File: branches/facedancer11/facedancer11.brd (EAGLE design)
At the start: 71.1 x 23.5 mm, 20 parts, among them CN1 HOST, CN2 VICTIM, Q1 12MHz, U1 F261X---PM64, U2 FT232RL-BASICSSOP, U3 MAX3420ELQFP32

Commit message: Facedancer11 pieces.
git-svn-id: https://svn.code.sf.net/p/goodfet/code@1181 12e2690d-a6be-4b82-a7b7-67c4a43b65c8
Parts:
- CN2: value VICTIM -> TARGET
- moved C6 2.81 mm to (53.8, 7.20)
- moved C7 1.61 mm to (42.4, 7.80)
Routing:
- net N$4: track 12.0 -> 14.7 mm
- net N$3: track 8.26 -> 10.1 mm
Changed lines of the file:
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@@
 <attribute name="VALUE" x="57.8635" y="0.18" size="1.27" layer="27" ratio="10" rot="R90"/>
 </element>
-<element name="CN2" library="adafruit" package="USB-MINIB" value="VICTIM" x="66.3575" y="9.8425" smashed="yes" rot="R90">
+<element name="CN2" library="adafruit" package="USB-MINIB" value="TARGET" x="66.3575" y="9.8425" smashed="yes" rot="R90">
 <attribute name="VALUE" x="62.45" y="15.775" size="1.27" layer="27"/>
 </element>
@@
 <attribute name="VALUE" x="55.36" y="16.6825" size="0.4064" layer="27" font="vector"/>
 </element>
-<element name="C6" library="rcl" package="C0603" value="18pF" x="51" y="7.4" smashed="yes" rot="R180">
-<attribute name="NAME" x="52.565" y="7.035" size="0.4064" layer="25" font="vector"/>
-</element>
-<element name="C7" library="rcl" package="C0603" value="18pF" x="44" y="7.6" smashed="yes">
-<attribute name="NAME" x="43.365" y="8.235" size="0.4064" layer="25" font="vector"/>
-<attribute name="VALUE" x="43.365" y="8.695" size="0.4064" layer="27" font="fixed"/>
+<element name="C6" library="rcl" package="C0603" value="18pF" x="53.8" y="7.2" smashed="yes" rot="R180">
+<attribute name="NAME" x="55.365" y="6.835" size="0.4064" layer="25" font="vector"/>
+</element>
+<element name="C7" library="rcl" package="C0603" value="18pF" x="42.4" y="7.8" smashed="yes">
+<attribute name="NAME" x="41.765" y="8.435" size="0.4064" layer="25" font="vector"/>
+<attribute name="VALUE" x="41.765" y="8.895" size="0.4064" layer="27" font="fixed"/>
 </element>
 </elements>
@@
 <contactref element="C7" pad="1"/>
 <contactref element="C6" pad="1"/>
-<wire x1="43.15" y1="7.6" x2="42.15" y2="7.55" width="0.254" layer="1"/>
-<wire x1="42.15" y1="7.55" x2="41" y2="6.8" width="0.254" layer="1"/>
-<via x="41" y="6.8" extent="1-16" drill="0.6"/>
-<wire x1="51.85" y1="7.4" x2="53.6" y2="7.4" width="0.254" layer="1"/>
-<wire x1="53.6" y1="7.4" x2="54" y2="8.2" width="0.254" layer="1"/>
-<via x="54" y="8.2" extent="1-16" drill="0.6"/>
+<wire x1="54.65" y1="7.2" x2="56.4" y2="6.8" width="0.254" layer="1"/>
+<wire x1="56.4" y1="6.8" x2="56.8" y2="6.4" width="0.254" layer="1"/>
+<via x="56.8" y="6.4" extent="1-16" drill="0.6"/>
 <contactref element="U3" pad="P18"/>
 <contactref element="U3" pad="P19"/>
@@
 <wire x1="53.3775" y1="14.435" x2="55.3675" y2="14.435" width="0.3048" layer="1"/>
 <wire x1="55.3675" y1="14.435" x2="56.1875" y2="15.255" width="0.3048" layer="1"/>
+<wire x1="41.55" y1="7.8" x2="40.6" y2="6.85" width="0.3048" layer="1"/>
+<wire x1="40.6" y1="6.85" x2="40.6" y2="6" width="0.3048" layer="1"/>
+<via x="40.6" y="6" extent="1-16" drill="0.6"/>
 </signal>
 <signal name="N$1">
@@
 <contactref element="Q1" pad="1"/>
 <contactref element="U3" pad="P26"/>
-<wire x1="46.7425" y1="8.7" x2="46.7425" y2="7.4" width="0.254" layer="1"/>
-<wire x1="46.7425" y1="7.4" x2="46.7425" y2="6.801" width="0.254" layer="1"/>
-<wire x1="46.7425" y1="6.801" x2="44.069" y2="3.3275" width="0.254" layer="1"/>
+<wire x1="46.7425" y1="8.7" x2="46.7425" y2="6.801" width="0.254" layer="1"/>
+<wire x1="46.7425" y1="6.801" x2="46.592334375" y2="6.6059" width="0.254" layer="1"/>
 <contactref element="C7" pad="2"/>
-<wire x1="44.85" y1="7.6" x2="46.5425" y2="7.6" width="0.254" layer="1"/>
-<wire x1="46.5425" y1="7.6" x2="46.7425" y2="7.4" width="0.254" layer="1"/>
+<wire x1="46.592334375" y1="6.6059" x2="44.069" y2="3.3275" width="0.254" layer="1"/>
+<wire x1="43.25" y1="7.8" x2="44.4441" y2="6.6059" width="0.3048" layer="1"/>
+<wire x1="44.4441" y1="6.6059" x2="46.592334375" y2="6.6059" width="0.3048" layer="1"/>
 </signal>
 <signal name="N$4">
@@
 <contactref element="C6" pad="2"/>
 <wire x1="47.5425" y1="7.2325" x2="49.9825" y2="7.2325" width="0.254" layer="1"/>
-<wire x1="49.9825" y1="7.2325" x2="50.15" y2="7.4" width="0.254" layer="1"/>
+<wire x1="49.9825" y1="7.2325" x2="52.95" y2="7.2" width="0.254" layer="1"/>
 </signal>
 <signal name="N$5">

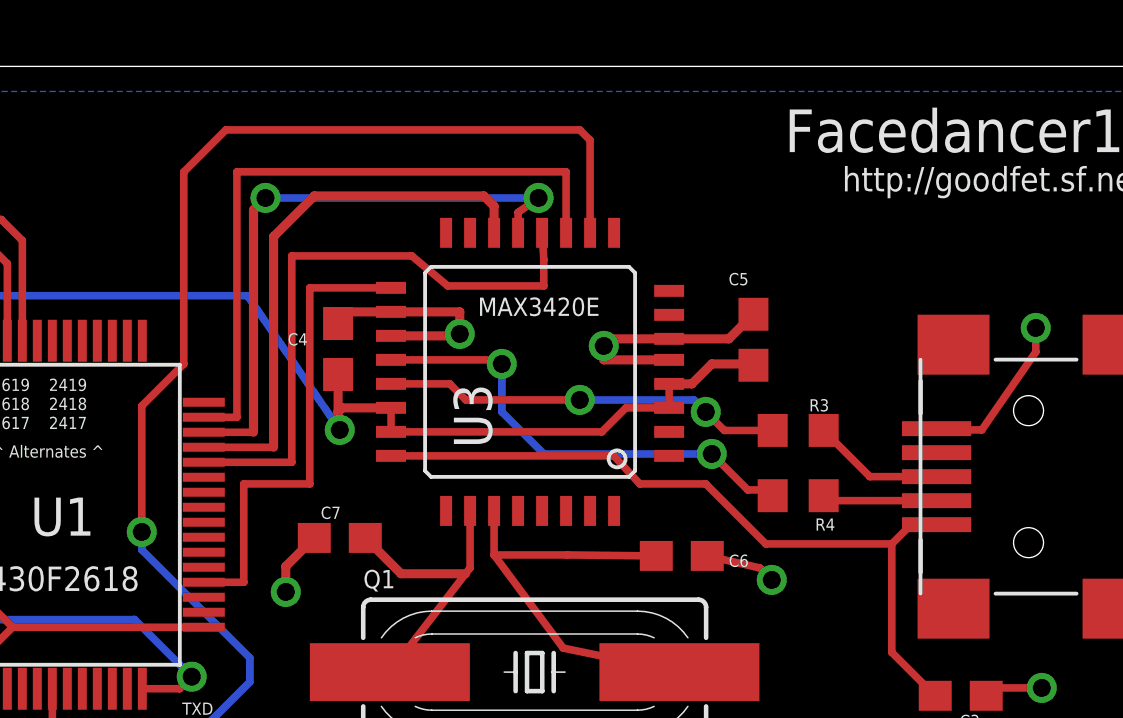
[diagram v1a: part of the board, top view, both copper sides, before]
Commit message: Improved Facedancer11 layout.
git-svn-id: https://svn.code.sf.net/p/goodfet/code@1184 12e2690d-a6be-4b82-a7b7-67c4a43b65c8
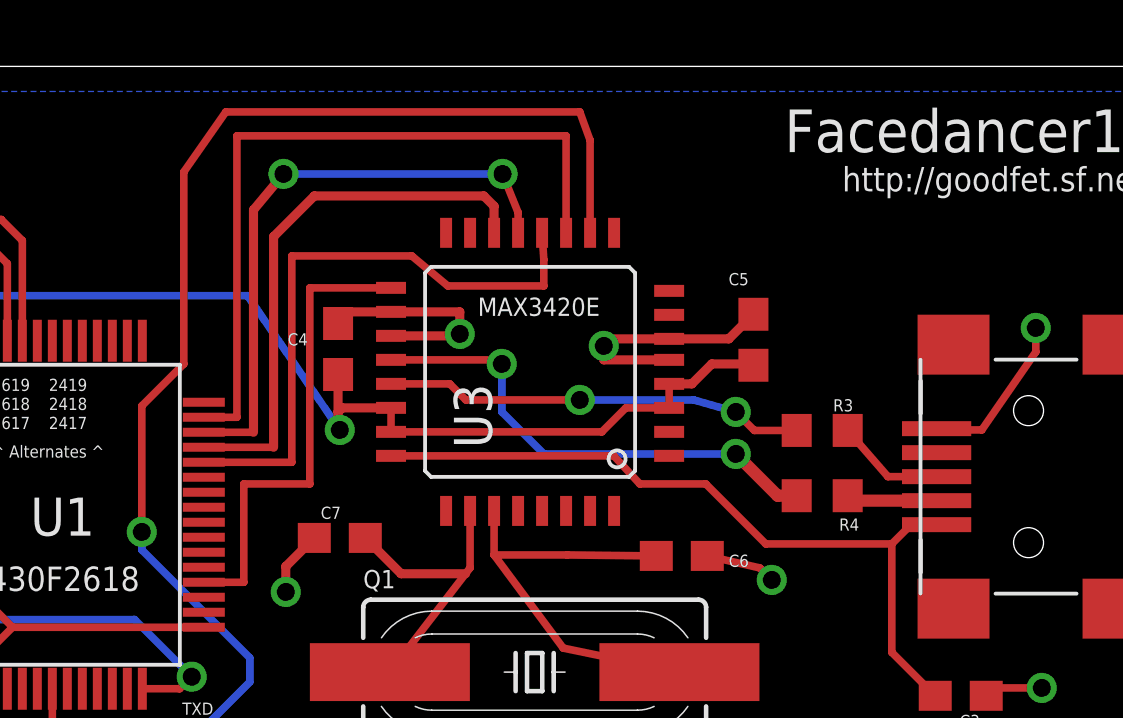
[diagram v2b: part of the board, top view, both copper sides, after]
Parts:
- moved R3 0.80 mm to (58.5, 11.4)
- moved R4 0.80 mm to (58.5, 9.21)
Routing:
- net SCLK: track 22.3 -> 24.7 mm
- net !RST: track 45.5 -> 46.5 mm
- net N$10: track 3.98 -> 3.13 mm
- net N$11: track 4.40 -> 3.66 mm
- net N$9: track 15.6 -> 16.3 mm
- net N$5: track 13.4 -> 14.1 mm
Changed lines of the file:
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@@
 <attribute name="VALUE" x="62.45" y="15.775" size="1.27" layer="27"/>
 </element>
-<element name="R3" library="rcl" package="R0603" value="33" x="57.68" y="11.3825" smashed="yes">
-<attribute name="NAME" x="58.045" y="12.0175" size="0.4064" layer="25" font="vector"/>
-<attribute name="VALUE" x="58.045" y="12.6775" size="0.4064" layer="27" font="vector"/>
-</element>
-<element name="R4" library="rcl" package="R0603" value="33" x="57.68" y="9.2075" smashed="yes">
-<attribute name="NAME" x="58.245" y="8.0425" size="0.4064" layer="25" font="vector"/>
-<attribute name="VALUE" x="58.245" y="7.5025" size="0.4064" layer="27" font="vector"/>
+<element name="R3" library="rcl" package="R0603" value="33" x="58.48" y="11.3825" smashed="yes">
+<attribute name="NAME" x="58.845" y="12.0175" size="0.4064" layer="25" font="vector"/>
+<attribute name="VALUE" x="58.845" y="12.6775" size="0.4064" layer="27" font="vector"/>
+</element>
+<element name="R4" library="rcl" package="R0603" value="33" x="58.48" y="9.2075" smashed="yes">
+<attribute name="NAME" x="59.045" y="8.0425" size="0.4064" layer="25" font="vector"/>
+<attribute name="VALUE" x="59.045" y="7.5025" size="0.4064" layer="27" font="vector"/>
 </element>
 <element name="C3" library="rcl" package="C0603" value="1.0uF" x="63.0975" y="2.5375" smashed="yes" rot="R180">
@@
 <contactref element="U3" pad="P13"/>
 <wire x1="37.8675" y1="11.3225" x2="39.5225" y2="11.3225" width="0.254" layer="1"/>
-<via x="39.9225" y="19.1325" extent="1-16" drill="0.6"/>
-<wire x1="39.9225" y1="19.1325" x2="49.025" y2="19.1325" width="0.254" layer="16"/>
+<via x="40.5225" y="19.9325" extent="1-16" drill="0.6"/>
+<wire x1="40.5225" y1="19.9325" x2="47.825" y2="19.9325" width="0.254" layer="16"/>
 <wire x1="48.3425" y1="17.97" x2="48.3425" y2="18.65" width="0.254" layer="1"/>
-<wire x1="48.3425" y1="18.65" x2="49.025" y2="19.1325" width="0.254" layer="1"/>
-<via x="49.025" y="19.1325" extent="1-16" drill="0.6"/>
+<wire x1="48.3425" y1="18.65" x2="47.825" y2="19.9325" width="0.254" layer="1"/>
+<via x="47.825" y="19.9325" extent="1-16" drill="0.6"/>
 <wire x1="39.5225" y1="11.3225" x2="39.5225" y2="18.7325" width="0.3048" layer="1"/>
-<wire x1="39.5225" y1="18.7325" x2="39.9225" y2="19.1325" width="0.3048" layer="1"/>
+<wire x1="39.5225" y1="18.7325" x2="40.5225" y2="19.9325" width="0.3048" layer="1"/>
 </signal>
 <signal name="SCLK">
@@
 <contactref element="U3" pad="P11"/>
 <wire x1="37.8675" y1="11.8225" x2="38.97" y2="11.8225" width="0.254" layer="1"/>
-<wire x1="38.97" y1="11.8225" x2="38.97" y2="20.0025" width="0.254" layer="1"/>
-<wire x1="38.97" y1="20.0025" x2="49.9425" y2="20.0025" width="0.254" layer="1"/>
-<wire x1="49.9425" y1="20.0025" x2="49.9425" y2="17.97" width="0.254" layer="1"/>
+<wire x1="38.97" y1="11.8225" x2="38.97" y2="21.2025" width="0.254" layer="1"/>
+<wire x1="38.97" y1="21.2025" x2="49.9425" y2="21.2025" width="0.254" layer="1"/>
+<wire x1="49.9425" y1="21.2025" x2="49.9425" y2="17.97" width="0.254" layer="1"/>
 </signal>
 <signal name="VCC">
@@
 <contactref element="U3" pad="P10"/>
 <wire x1="50.7425" y1="17.97" x2="50.7425" y2="21.0575" width="0.254" layer="1"/>
-<wire x1="50.7425" y1="21.0575" x2="50.4" y2="21.4" width="0.254" layer="1"/>
-<wire x1="50.4" y1="21.4" x2="38.6" y2="21.4" width="0.254" layer="1"/>
-<wire x1="38.6" y1="21.4" x2="37.2" y2="20" width="0.254" layer="1"/>
+<wire x1="50.7425" y1="21.0575" x2="50.4" y2="22" width="0.254" layer="1"/>
+<wire x1="50.4" y1="22" x2="38.6" y2="22" width="0.254" layer="1"/>
+<wire x1="38.6" y1="22" x2="37.2" y2="20" width="0.254" layer="1"/>
 <wire x1="37.2" y1="20" x2="37.2" y2="13.6" width="0.254" layer="1"/>
 <wire x1="37.2" y1="13.6" x2="35.8" y2="12.2" width="0.254" layer="1"/>
@@
 <via x="50.4" y="12.4" extent="1-16" drill="0.6"/>
 <wire x1="50.4" y1="12.4" x2="54.2" y2="12.4" width="0.254" layer="16"/>
-<wire x1="54.2" y1="12.4" x2="54.6" y2="12" width="0.254" layer="16"/>
-<wire x1="56.83" y1="11.3825" x2="55.2175" y2="11.3825" width="0.254" layer="1"/>
-<wire x1="55.2175" y1="11.3825" x2="54.6" y2="12" width="0.254" layer="1"/>
-<via x="54.6" y="12" extent="1-16" drill="0.6"/>
+<wire x1="54.2" y1="12.4" x2="55.6" y2="12" width="0.254" layer="16"/>
+<wire x1="57.63" y1="11.3825" x2="56.2175" y2="11.3825" width="0.254" layer="1"/>
+<wire x1="56.2175" y1="11.3825" x2="55.6" y2="12" width="0.254" layer="1"/>
+<via x="55.6" y="12" extent="1-16" drill="0.6"/>
 </signal>
 <signal name="N$9">
@@
 <wire x1="47.8" y1="13.6" x2="47.8" y2="12" width="0.254" layer="16"/>
 <wire x1="47.8" y1="12" x2="49.2" y2="10.6" width="0.254" layer="16"/>
-<wire x1="49.2" y1="10.6" x2="54.8" y2="10.6" width="0.254" layer="16"/>
-<wire x1="56.83" y1="9.2075" x2="56.83" y2="9.37" width="0.254" layer="1"/>
-<wire x1="56.83" y1="9.37" x2="56.8" y2="9.4" width="0.254" layer="1"/>
-<wire x1="56.8" y1="9.4" x2="56" y2="9.4" width="0.254" layer="1"/>
-<wire x1="56" y1="9.4" x2="54.8" y2="10.6" width="0.254" layer="1"/>
-<via x="54.8" y="10.6" extent="1-16" drill="0.6"/>
+<wire x1="49.2" y1="10.6" x2="55.6" y2="10.6" width="0.254" layer="16"/>
+<via x="55.6" y="10.6" extent="1-16" drill="0.6"/>
+<wire x1="57.63" y1="9.2075" x2="56.9925" y2="9.2075" width="0.4064" layer="1"/>
+<wire x1="56.9925" y1="9.2075" x2="55.6" y2="10.6" width="0.4064" layer="1"/>
 </signal>
 <signal name="VBCOMP">
@@
 <contactref element="CN2" pad="D-"/>
 <contactref element="R4" pad="2"/>
-<wire x1="58.53" y1="9.36" x2="58.53" y2="9.2075" width="0.254" layer="1"/>
-<wire x1="62.2935" y1="9.0425" x2="58.7575" y2="9.0425" width="0.254" layer="1"/>
-<wire x1="58.7575" y1="9.0425" x2="58.6" y2="9.2" width="0.254" layer="1"/>
-<wire x1="58.6" y1="9.2" x2="58.5375" y2="9.2" width="0.254" layer="1"/>
-<wire x1="58.5375" y1="9.2" x2="58.53" y2="9.2075" width="0.254" layer="1"/>
+<wire x1="62.2935" y1="9.0425" x2="59.33" y2="9.0425" width="0.4064" layer="1"/>
+<wire x1="59.33" y1="9.0425" x2="59.33" y2="9.2075" width="0.4064" layer="1"/>
 </signal>
 <signal name="N$11">
 <contactref element="CN2" pad="D+"/>
 <contactref element="R3" pad="2"/>
-<wire x1="62.2935" y1="9.8425" x2="60.07" y2="9.8425" width="0.254" layer="1"/>
-<wire x1="60.07" y1="9.8425" x2="58.53" y2="11.3825" width="0.254" layer="1"/>
+<wire x1="62.2935" y1="9.8425" x2="60.67" y2="9.8425" width="0.254" layer="1"/>
+<wire x1="60.67" y1="9.8425" x2="59.33" y2="11.3825" width="0.254" layer="1"/>
 </signal>
 </signals>
